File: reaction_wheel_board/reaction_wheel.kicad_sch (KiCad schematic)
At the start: 18 parts, among them U1 DRV8317HREER

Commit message: pcb layouts
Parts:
- removed C10, C13: 10μF, symbol Device:C_Polarized_US
- removed R1, R2, R3: 330R, symbol Device:R
- added C10, C12: 10μF, Capacitor_SMD:C_0603_1608Metric, symbol Device:C
- added R1, R2: 330, Resistor_SMD:R_0603_1608Metric, symbol Device:R_US
- added R3, R7: 0R, Resistor_SMD:R_0603_1608Metric, symbol Device:R_US
- added R8: 47k, Resistor_SMD:R_0603_1608Metric, symbol Device:R_US
- C1, C11, C2, C3, C4, C5, C6, C7, C8, C9: footprint (none) -> Capacitor_SMD:C_0603_1608Metric
- R4: value R_US -> 330; footprint (none) -> Resistor_SMD:R_0603_1608Metric
- R5: footprint (none) -> Resistor_SMD:R_0603_1608Metric
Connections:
- net +12V: now also C11.2, C6.2, C10.2, C12.2; no longer C11.1, C6.1
- net +3.3V: now also R3.2
- net ADC_A: now also C2.1, R4.2; no longer C1.1
- net ADC_B: now also C1.1, R1.2; no longer C2.1
- net ADC_C: now also R2.2
- net GND: now also C11.1, C6.1, C10.1, C12.1, R7.1, R8.1; no longer C11.2, C6.2
- net at R4.1: now also U1.36 (SOA)
- net at U1.34 (SOC): now also R2.1
- net at U1.35 (SOB): now also R1.1
- net GAIN: no longer names the net of U1.29 (GAIN)
- net GAIN: now also R3.1, R7.2, R8.2
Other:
- moved on the sheet: R4

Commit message: mostly finished pcb
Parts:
- added J1: PWM Pins, Connector_PinSocket_2.54mm:PinSocket_1x06_P2.54mm_Vertical, symbol Connector_Generic_MountingPin:Conn_01x06_MountingPin
- added J2: Current Sense Pins, Connector_PinSocket_2.54mm:PinSocket_1x03_P2.54mm_Vertical, symbol Connector_Generic_MountingPin:Conn_01x03_MountingPin
- added J3: Motor Out Pins, Connector_PinSocket_2.54mm:PinSocket_1x03_P2.54mm_Vertical, symbol Connector_Generic_MountingPin:Conn_01x03_MountingPin
- added J4: Power Pins, Connector_PinSocket_2.54mm:PinSocket_1x03_P2.54mm_Vertical, symbol Connector_Generic_MountingPin:Conn_01x03_MountingPin
- 47n1: renamed from C4; value 22pF -> 47nF
- U1: footprint WQFN36_REE_TEX -> DRV8317HREER:WQFN36_REE_TEX
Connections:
- net +1V8 is gone; now on net +3.3V: C9.2, U1.33 (CSAREF)
- net +12V: now also J4.3 (Pin_3)
- net +3.3V: now also J4.2 (Pin_2)
- net ADC_A: now also J2.1 (Pin_1)
- net ADC_B: now also J2.2 (Pin_2)
- net ADC_C: now also J2.3 (Pin_3)
- net GND: now also J4.1 (Pin_1)
- net OUT_A: now also J3.3 (Pin_3)
- net OUT_B: now also J3.2 (Pin_2)
- net OUT_C: now also J3.1 (Pin_1)
- net PWM_H_A: now also J1.6 (Pin_6)
- net PWM_H_B: now also J1.4 (Pin_4)
- net PWM_H_C: now also J1.2 (Pin_2)
- net PWM_L_A: now also J1.5 (Pin_5)
- net PWM_L_B: now also J1.3 (Pin_3)
- net PWM_L_C: now also J1.1 (Pin_1)
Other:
- moved on the sheet: R3

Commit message: i think its done
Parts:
- removed J2: Current Sense Pins, Connector_PinSocket_2.54mm:PinSocket_1x03_P2.54mm_Vertical, symbol Connector_Generic_MountingPin:Conn_01x03_MountingPin
- removed J3: Motor Out Pins, Connector_PinSocket_2.54mm:PinSocket_1x03_P2.54mm_Vertical, symbol Connector_Generic_MountingPin:Conn_01x03_MountingPin
- added J2: Conn_01x05, Connector_PinHeader_2.54mm:PinHeader_1x05_P2.54mm_Vertical, symbol Connector_Generic:Conn_01x05
- added J3, J5: Screw_Terminal_01x02, ssi_connector:1985807, symbol Connector:Screw_Terminal_01x02
- J1: footprint Connector_PinSocket_2.54mm:PinSocket_1x06_P2.54mm_Vertical -> Connector_PinHeader_2.54mm:PinHeader_1x06_P2.54mm_Vertical
- J4: footprint Connector_PinSocket_2.54mm:PinSocket_1x03_P2.54mm_Vertical -> Connector_PinHeader_2.54mm:PinHeader_1x03_P2.54mm_Vertical
- U1: footprint DRV8317HREER:WQFN36_REE_TEX -> ssi_driver:QFN-36_EP_4.6x5.4_Pitch0.4mm
- renumbered 47n1 to C4
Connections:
- net +3.3V: now also C8.2, R5.1, J2.2 (Pin_2); no longer C8.1
- net ADC_A: now also J2.5 (Pin_5)
- net ADC_B: now also J2.4 (Pin_4)
- net ADC_C: now also J2.3 (Pin_3)
- net GND: now also C8.1, U1.10 (PGND), U1.13 (PGND), U1.16 (PGND), J2.1 (Pin_1), J5.1 (Pin_1)
- net OUT_A: now also J5.2 (Pin_2)
- net OUT_B: now also J3.1 (Pin_1)
- net OUT_C: now also J3.2 (Pin_2)
- no-connect marks 3 -> 4
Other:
- moved on the sheet: C8

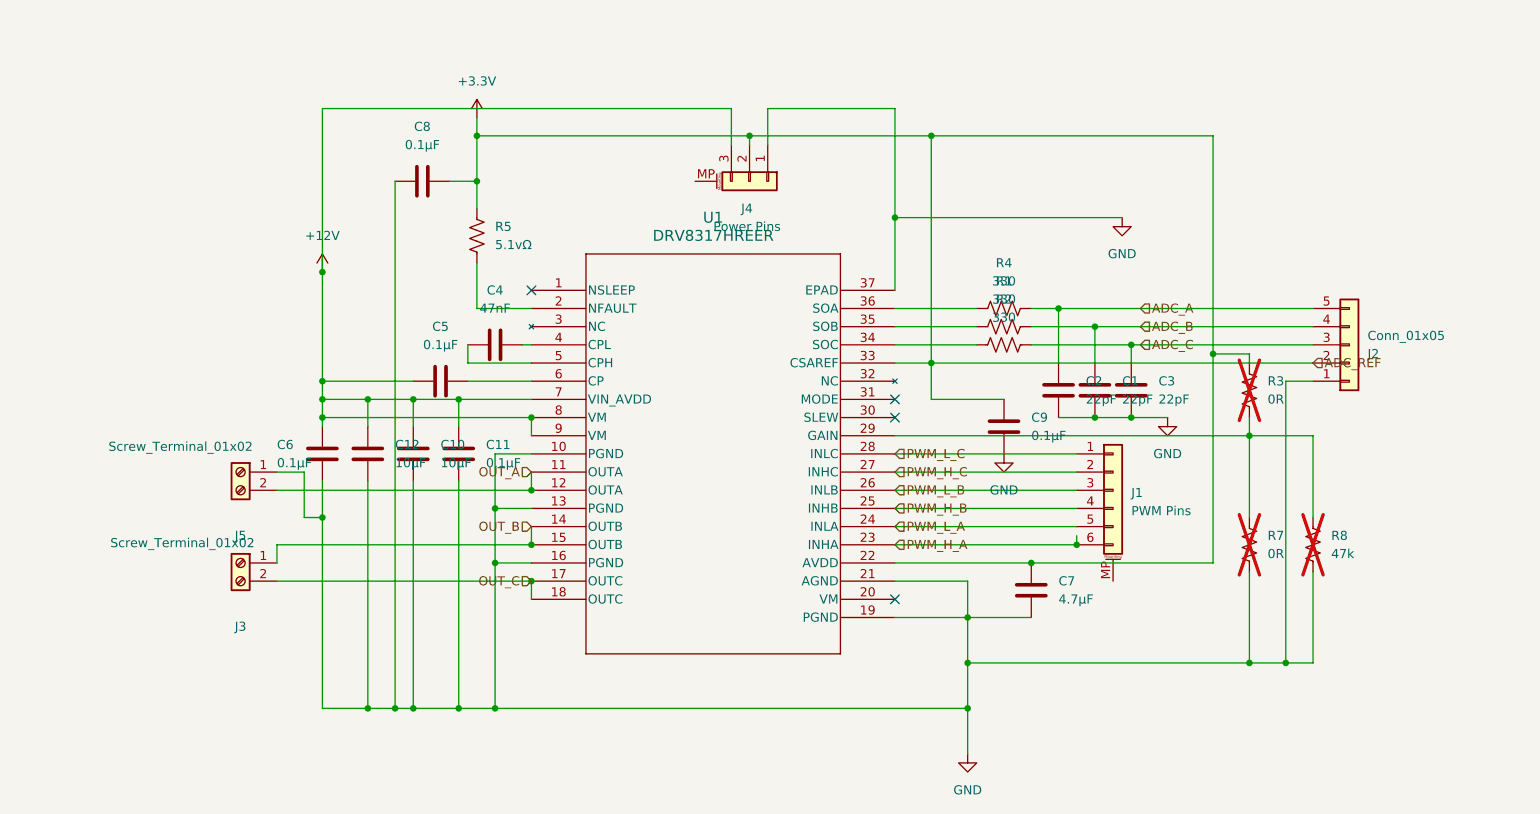
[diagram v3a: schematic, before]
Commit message: Cleaned up reaction wheel board schematic
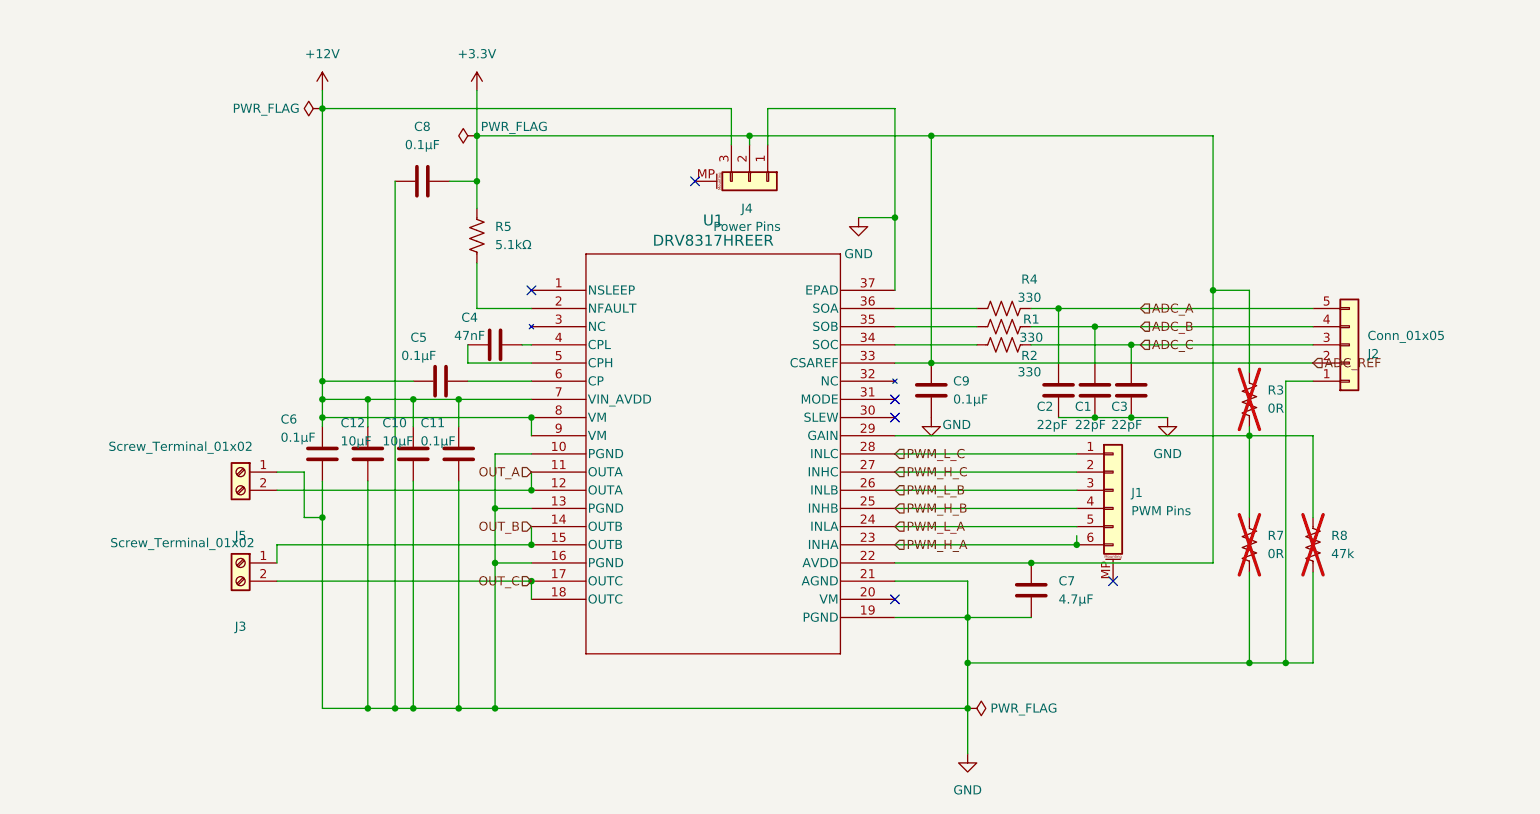
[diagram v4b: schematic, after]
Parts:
- R5: value 5.1vΩ -> 5.1kΩ
- U1: symbol DRV8317HREER:DRV8317HREER -> ssi_IC:DRV8317HREER
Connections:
- no-connect marks 4 -> 6
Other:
- title: (none) -> Reaction Wheel Board
- moved on the sheet: C9, R3

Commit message: reaction wheel board finish
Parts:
- J1: symbol Connector_Generic_MountingPin:Conn_01x06_MountingPin -> Connector_Generic:Conn_01x06
- J4: symbol Connector_Generic_MountingPin:Conn_01x03_MountingPin -> Connector_Generic:Conn_01x03
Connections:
- no-connect marks 6 -> 4
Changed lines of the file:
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@@
 	(title_block
 		(title "Reaction Wheel Board")
-		(date "2024-12-03")
+		(date "2024-12-07")
 		(rev "v1a")
 		(comment 1 "Carson Lauer")
@@
 	(no_connect
 		(at 142.24 101.6)
-	)
-	(no_connect
-		(at 172.72 99.06)
-	)
-	(no_connect
-		(at 114.3 43.18)
 	)
 	(no_connect
@@
 	)
 	(symbol
-		(lib_id "Connector_Generic_MountingPin:Conn_01x03_MountingPin")
+		(lib_id "Connector_Generic:Conn_01x03")
 		(at 121.92 43.18 270)
 		(unit 1)
@@
 		(fields_autoplaced yes)
 		(property "Reference" "J4"
-			(at 121.5644 46.99 90)
-			(effects
-				(font
-					(size 1.27 1.27)
-				)
+			(at 127 41.9099 90)
+			(effects
+				(font
+					(size 1.27 1.27)
+				)
+				(justify left)
 			)
 		)
 		(property "Value" "Power Pins"
-			(at 121.5644 49.53 90)
-			(effects
-				(font
-					(size 1.27 1.27)
-				)
+			(at 127 44.4499 90)
+			(effects
+				(font
+					(size 1.27 1.27)
+				)
+				(justify left)
 			)
 		)
@@
 			)
 		)
-		(property "Description" "Generic connectable mounting pin connector, single row, 01x03, script generated (kicad-library-utils/schlib/autogen/connector/)"
+		(property "Description" "Generic connector, single row, 01x03, script generated (kicad-library-utils/schlib/autogen/connector/)"
 			(at 121.92 43.18 0)
 			(effects
@@
 		)
 		(pin "1"
-		)
-		(pin "MP"
 		)
 		(pin "3"
@@
 	)
 	(symbol
-		(lib_id "Connector_Generic_MountingPin:Conn_01x06_MountingPin")
+		(lib_id "Connector_Generic:Conn_01x06")
 		(at 172.72 86.36 0)
 		(unit 1)
@@
 		(fields_autoplaced yes)
 		(property "Reference" "J1"
-			(at 175.26 86.7155 0)
+			(at 175.26 86.3599 0)
 			(effects
 				(font
@@
 		)
 		(property "Value" "PWM Pins"
-			(at 175.26 89.2555 0)
+			(at 175.26 88.8999 0)
 			(effects
 				(font
@@
 			)
 		)
-		(property "Description" "Generic connectable mounting pin connector, single row, 01x06, script generated (kicad-library-utils/schlib/autogen/connector/)"
+		(property "Description" "Generic connector, single row, 01x06, script generated (kicad-library-utils/schlib/autogen/connector/)"
 			(at 172.72 86.36 0)
 			(effects
@@
 		(pin "4"
 		)
-		(pin "MP"
-		)
 		(instances

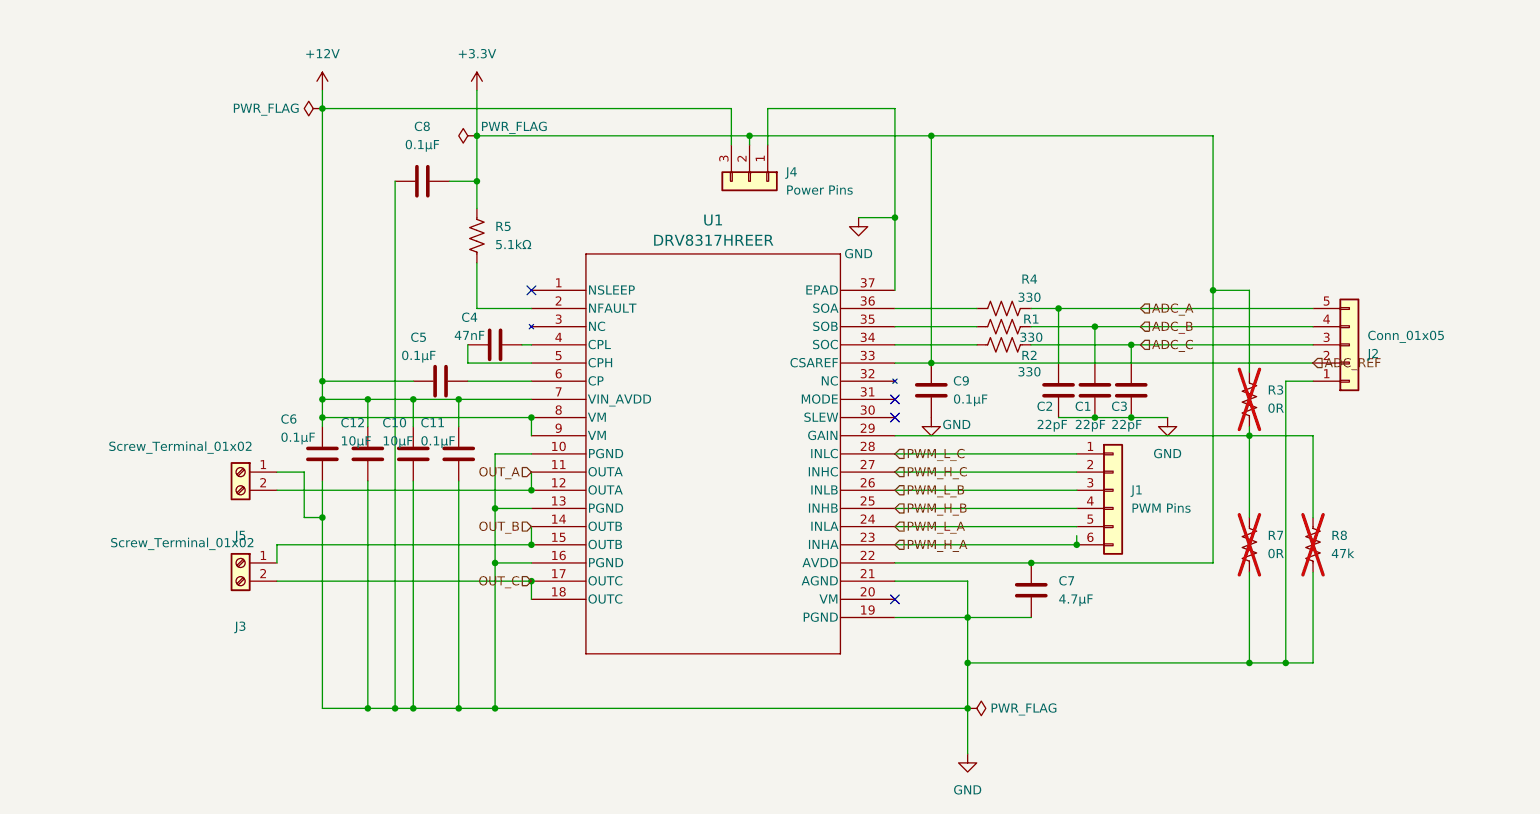
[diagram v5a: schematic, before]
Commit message: reaction wheel cleanup
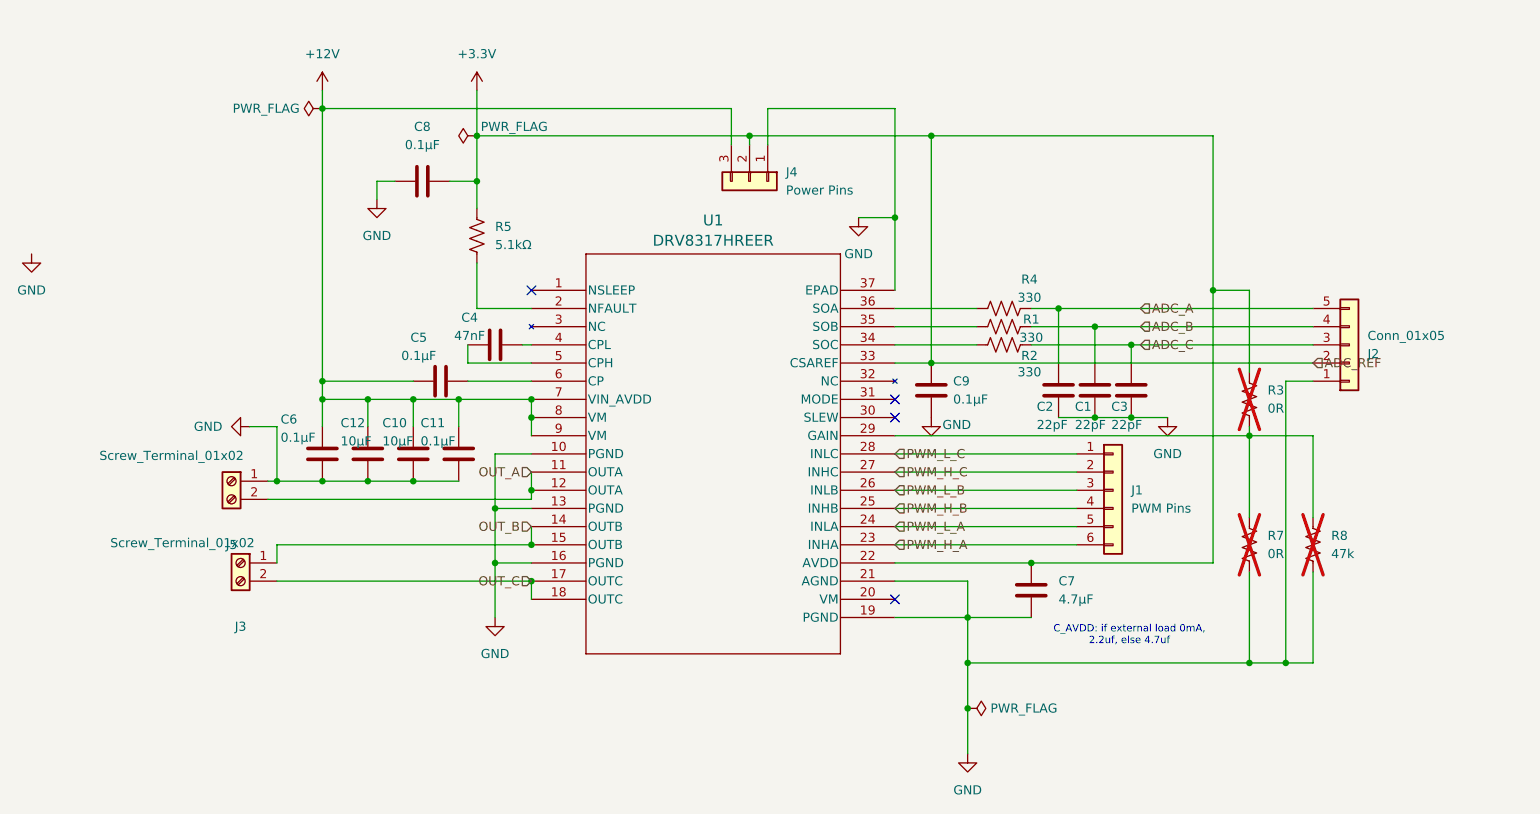
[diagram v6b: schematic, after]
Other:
- note added: "C_AVDD: if external load 0mA, 2.2uf, else 4.7uf"
- moved on the sheet: J5

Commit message: added sleep pin and fault pin for readout
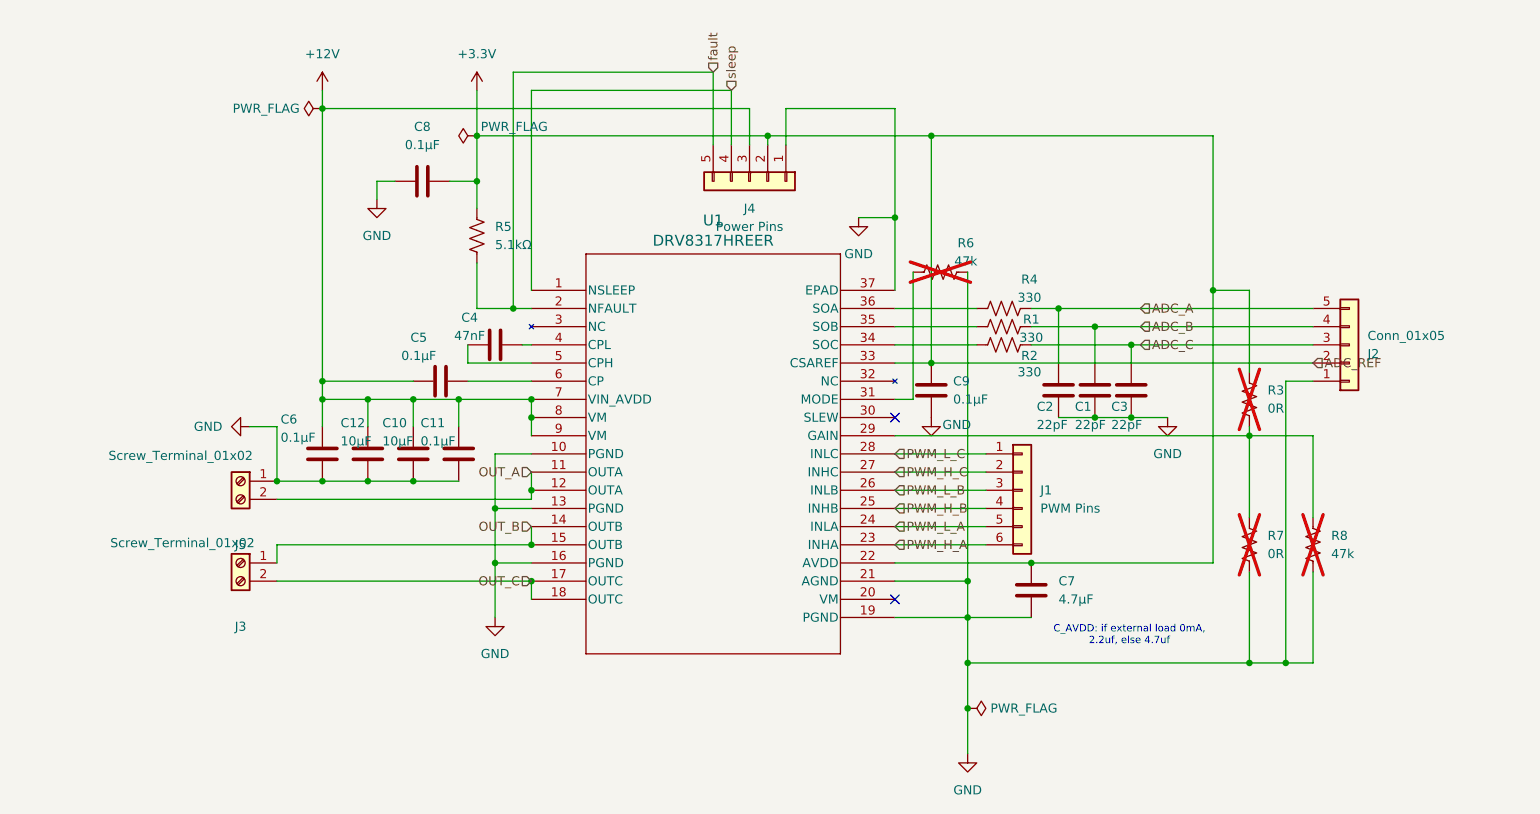
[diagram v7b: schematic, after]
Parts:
- added R6: 47k, Resistor_SMD:R_0603_1608Metric, symbol Device:R_US
- J4: footprint Connector_PinHeader_2.54mm:PinHeader_1x03_P2.54mm_Vertical -> Connector_PinHeader_2.54mm:PinHeader_1x05_P2.54mm_Vertical; symbol Connector_Generic:Conn_01x03 -> Connector_Generic:Conn_01x05
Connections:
- net GND: now also R6.2
- net sleep: now reaches U1.1 (NSLEEP)
- net sleep: now also J4.4 (Pin_4)
- net fault: now reaches R5.2, U1.2 (NFAULT)
- net fault: now also J4.5 (Pin_5)
- net at U1.31 (MODE): now also R6.1
- no-connect marks 4 -> 2
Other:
- moved on the sheet: J1, J5
